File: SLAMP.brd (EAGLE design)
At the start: 160 x 100 mm, 45 parts, among them IC1 MEGA8-AI, J1 CARA1, J2 CARA4, J3 CARA2, J4 CARA5, J5 CARA3, J6 EXTRA-D12, J7 A0, Q1 2N7002PW, U1 HC_05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

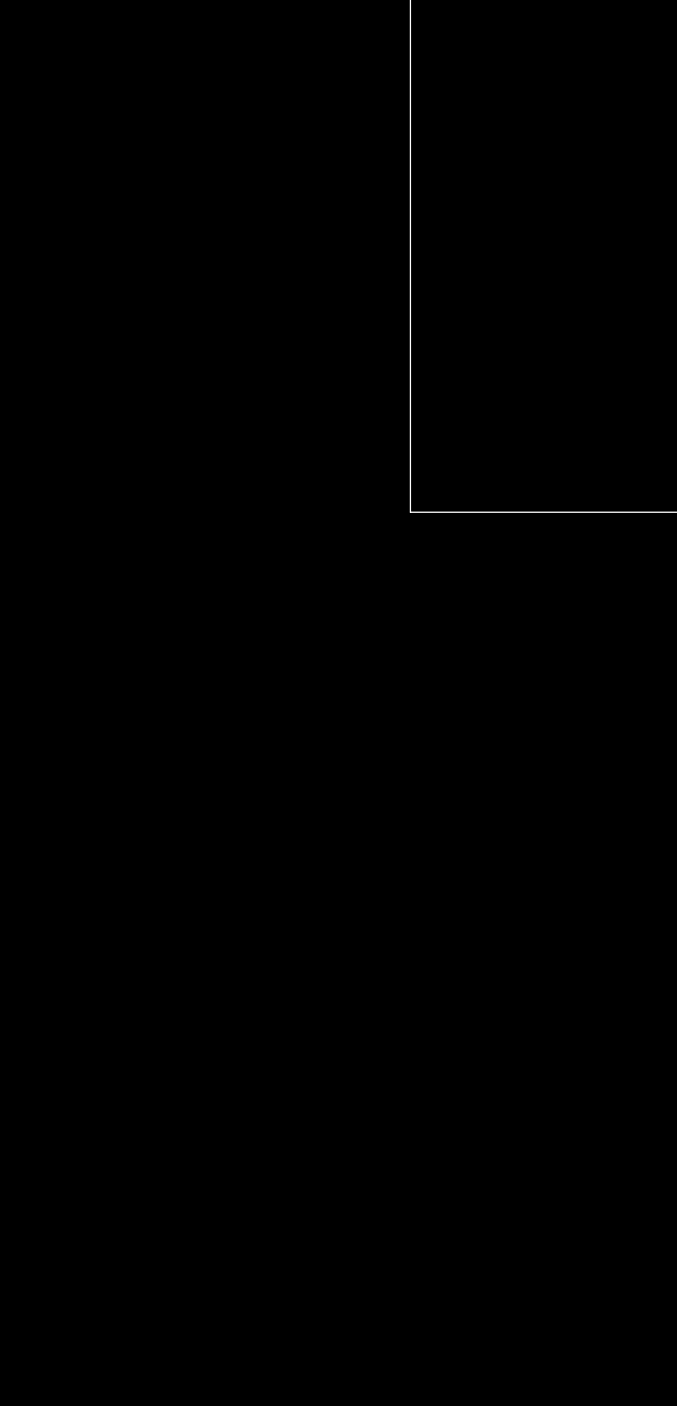
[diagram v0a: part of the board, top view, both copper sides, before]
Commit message: capacitive touch sensor added
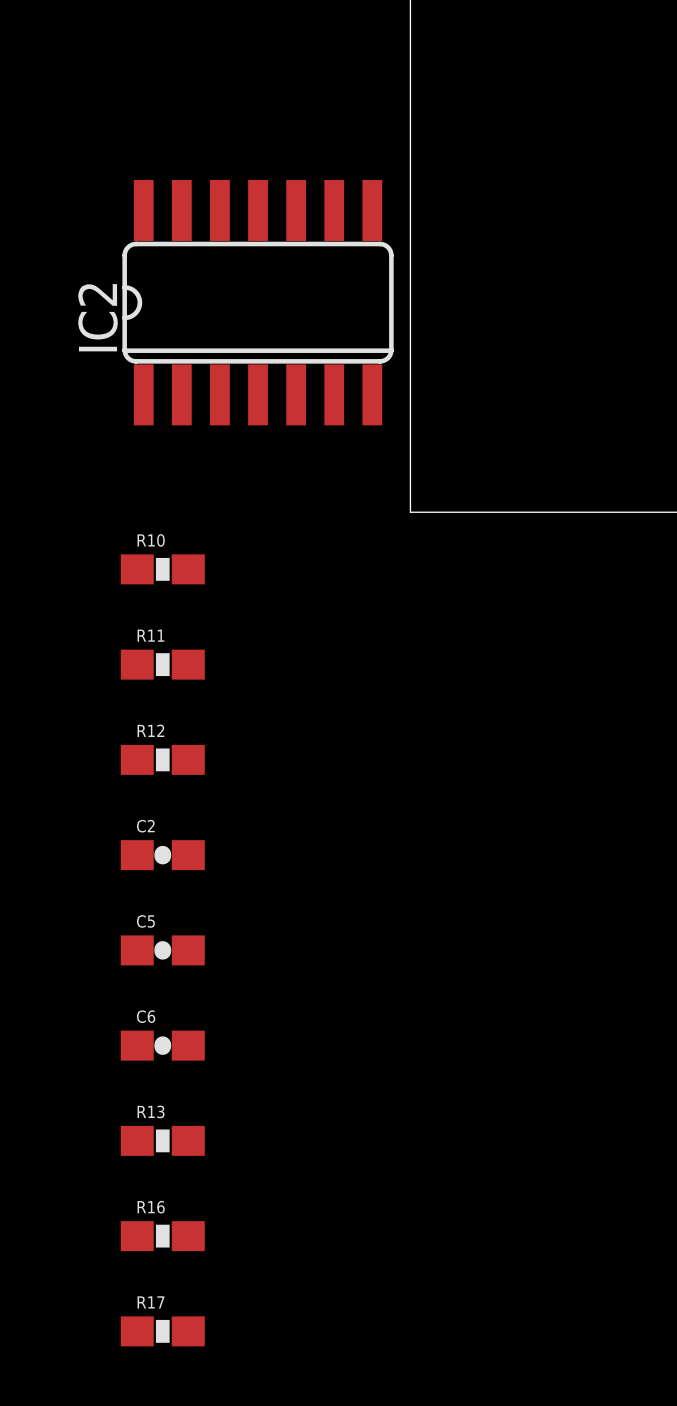
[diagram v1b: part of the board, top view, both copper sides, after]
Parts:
- added C2, C5: 1uF, SparkFun-Passives:0603-CAP
- added C6: 100nF, SparkFun-Passives:0603-CAP
- added IC2: AT42QT1070-SSU, adafruit:SO14
- added R10, R11, R12: 1k, SparkFun-Passives:0603-RES
- added R13, R16, R17: 10k, SparkFun-Passives:0603-RES
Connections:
- new net N$1: IC2.5, R17.2
- new net N$11: IC2.11, R12.1
- new net N$19: R10.2
- new net N$20: R11.2
- new net N$21: R12.2
- new net N$8: IC2.13, R10.1
- new net N$9: IC2.12, R11.1
- new net SCL: IC2.6, R16.2
- new net SDA: IC2.3, R13.2
- net 3.3V: now also C2.1, C5.1, C6.1, IC2.1, IC2.4, R13.1, R16.1, R17.1
- net GND: now also C2.2, C5.2, C6.2, IC2.14, IC2.2
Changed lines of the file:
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@@
 <?xml version="1.0" encoding="utf-8"?>
 <!DOCTYPE eagle SYSTEM "eagle.dtd">
-<eagle version="7.3.0">
+<eagle version="7.7.0">
 <drawing>
 <settings>
@@
 <attribute name="PROD_ID" value="XTAL-08900" x="42.545" y="78.105" size="1.778" layer="27" rot="R180" display="off"/>
 </element>
+<element name="IC2" library="adafruit" package="SO14" value="AT42QT1070-SSU" x="-5.08" y="6.985"/>
+<element name="R10" library="SparkFun-Passives" package="0603-RES" value="1k" x="-8.255" y="-1.905"/>
+<element name="R11" library="SparkFun-Passives" package="0603-RES" value="1k" x="-8.255" y="-5.08"/>
+<element name="R12" library="SparkFun-Passives" package="0603-RES" value="1k" x="-8.255" y="-8.255"/>
+<element name="C2" library="SparkFun-Passives" package="0603-CAP" value="1uF" x="-8.255" y="-11.43"/>
+<element name="C5" library="SparkFun-Passives" package="0603-CAP" value="1uF" x="-8.255" y="-14.605"/>
+<element name="C6" library="SparkFun-Passives" package="0603-CAP" value="100nF" x="-8.255" y="-17.78"/>
+<element name="R13" library="SparkFun-Passives" package="0603-RES" value="10k" x="-8.255" y="-20.955"/>
+<element name="R16" library="SparkFun-Passives" package="0603-RES" value="10k" x="-8.255" y="-24.13"/>
+<element name="R17" library="SparkFun-Passives" package="0603-RES" value="10k" x="-8.255" y="-27.305"/>
 </elements>
 <signals>
@@
 <wire x1="15.24" y1="78.105" x2="17.36" y2="78.105" width="0.254" layer="1"/>
 <wire x1="17.36" y1="78.105" x2="17.995" y2="78.74" width="0.254" layer="1"/>
+<wire x1="13.97" y1="43.815" x2="13.97" y2="46.62" width="0.254" layer="1"/>
+<wire x1="13.97" y1="46.62" x2="14.34" y2="46.99" width="0.254" layer="1"/>
+<wire x1="14.34" y1="46.99" x2="14.34" y2="47.255" width="0.254" layer="1"/>
+<wire x1="14.34" y1="47.255" x2="12.7" y2="48.895" width="0.254" layer="1"/>
+<wire x1="12.7" y1="48.895" x2="12.7" y2="51.435" width="0.254" layer="1"/>
+<wire x1="39.612" y1="57.15" x2="39.612" y2="59.055" width="0.254" layer="1"/>
+<wire x1="39.612" y1="59.055" x2="41.91" y2="59.055" width="0.254" layer="1"/>
+<wire x1="41.91" y1="59.055" x2="42.545" y2="59.69" width="0.254" layer="1"/>
+<wire x1="42.545" y1="59.69" x2="43.93" y2="59.69" width="0.254" layer="1"/>
+<wire x1="43.93" y1="59.69" x2="44.15" y2="59.91" width="0.254" layer="1"/>
+<wire x1="25.4" y1="77.47" x2="25.4" y2="79.07" width="0.254" layer="1"/>
+<wire x1="25.4" y1="79.07" x2="25.095" y2="79.375" width="0.254" layer="1"/>
+<contactref element="IC2" pad="14"/>
+<contactref element="IC2" pad="2"/>
+<contactref element="C2" pad="2"/>
+<contactref element="C5" pad="2"/>
+<contactref element="C6" pad="2"/>
 <wire x1="46.45" y1="85.81" x2="55.975" y2="85.81" width="0" layer="19" extent="1-1"/>
 <wire x1="42.545" y1="79.121" x2="46.45" y2="85.81" width="0" layer="19" extent="1-1"/>
@@
 <wire x1="17.995" y1="76.835" x2="24.4475" y2="76.5175" width="0" layer="19" extent="1-1"/>
 <wire x1="17.875" y1="85.81" x2="17.995" y2="80.01" width="0" layer="19" extent="1-1"/>
+<wire x1="27.4" y1="85.81" x2="25.095" y2="79.375" width="0" layer="19" extent="1-1"/>
 <wire x1="17.995" y1="68.58" x2="25.0825" y2="69.7103" width="0" layer="19" extent="1-1"/>
 <wire x1="11.9888" y1="62.5856" x2="17.995" y2="68.58" width="0" layer="19" extent="1-1"/>
-<wire x1="27.4" y1="85.81" x2="25.095" y2="79.375" width="0" layer="19" extent="1-1"/>
 <wire x1="12.7" y1="51.435" x2="11.9888" y2="62.5856" width="0" layer="19" extent="1-1"/>
-<wire x1="13.97" y1="43.815" x2="13.97" y2="46.62" width="0.254" layer="1"/>
-<wire x1="13.97" y1="46.62" x2="14.34" y2="46.99" width="0.254" layer="1"/>
-<wire x1="14.34" y1="46.99" x2="14.34" y2="47.255" width="0.254" layer="1"/>
-<wire x1="14.34" y1="47.255" x2="12.7" y2="48.895" width="0.254" layer="1"/>
-<wire x1="12.7" y1="48.895" x2="12.7" y2="51.435" width="0.254" layer="1"/>
-<wire x1="39.612" y1="57.15" x2="39.612" y2="59.055" width="0.254" layer="1"/>
-<wire x1="39.612" y1="59.055" x2="41.91" y2="59.055" width="0.254" layer="1"/>
-<wire x1="41.91" y1="59.055" x2="42.545" y2="59.69" width="0.254" layer="1"/>
-<wire x1="42.545" y1="59.69" x2="43.93" y2="59.69" width="0.254" layer="1"/>
-<wire x1="43.93" y1="59.69" x2="44.15" y2="59.91" width="0.254" layer="1"/>
-<wire x1="25.4" y1="77.47" x2="25.4" y2="79.07" width="0.254" layer="1"/>
-<wire x1="25.4" y1="79.07" x2="25.095" y2="79.375" width="0.254" layer="1"/>
+<wire x1="-8.89" y1="10.0584" x2="13.97" y2="43.815" width="0" layer="19" extent="1-1"/>
+<wire x1="-7.62" y1="3.9116" x2="-8.89" y2="10.0584" width="0" layer="19" extent="1-1"/>
+<wire x1="-7.405" y1="-11.43" x2="-7.62" y2="3.9116" width="0" layer="19" extent="1-1"/>
+<wire x1="-7.405" y1="-14.605" x2="-7.405" y2="-11.43" width="0" layer="19" extent="1-1"/>
+<wire x1="-7.405" y1="-17.78" x2="-7.405" y2="-14.605" width="0" layer="19" extent="1-1"/>
 </signal>
 <signal name="DTR">
@@
 <via x="37.465" y="67.945" extent="1-16" drill="0.6"/>
 <wire x1="37.465" y1="67.945" x2="35.775" y2="67.945" width="0.254" layer="1"/>
+<contactref element="IC2" pad="4"/>
+<contactref element="C2" pad="1"/>
+<contactref element="C5" pad="1"/>
+<contactref element="C6" pad="1"/>
+<contactref element="R13" pad="1"/>
+<contactref element="R16" pad="1"/>
+<contactref element="R17" pad="1"/>
+<contactref element="IC2" pad="1"/>
+<wire x1="-5.08" y1="3.9116" x2="22.5425" y2="65.405" width="0" layer="19" extent="1-1"/>
+<wire x1="-8.89" y1="3.9116" x2="-5.08" y2="3.9116" width="0" layer="19" extent="1-1"/>
+<wire x1="-9.105" y1="-11.43" x2="-8.89" y2="3.9116" width="0" layer="19" extent="1-1"/>
+<wire x1="-9.105" y1="-14.605" x2="-9.105" y2="-11.43" width="0" layer="19" extent="1-1"/>
+<wire x1="-9.105" y1="-17.78" x2="-9.105" y2="-14.605" width="0" layer="19" extent="1-1"/>
+<wire x1="-9.105" y1="-20.955" x2="-9.105" y2="-17.78" width="0" layer="19" extent="1-1"/>
+<wire x1="-9.105" y1="-24.13" x2="-9.105" y2="-20.955" width="0" layer="19" extent="1-1"/>
+<wire x1="-9.105" y1="-27.305" x2="-9.105" y2="-24.13" width="0" layer="19" extent="1-1"/>
 </signal>
 <signal name="B1">
@@
 <wire x1="26.9875" y1="73.66" x2="26.9875" y2="75.0697" width="0.254" layer="1"/>
 </signal>
+<signal name="N$8">
+<contactref element="IC2" pad="13"/>
+<contactref element="R10" pad="1"/>
+<wire x1="-7.62" y1="10.0584" x2="-9.105" y2="-1.905" width="0" layer="19" extent="1-1"/>
+</signal>
+<signal name="N$9">
+<contactref element="IC2" pad="12"/>
+<contactref element="R11" pad="1"/>
+<wire x1="-6.35" y1="10.0584" x2="-9.105" y2="-5.08" width="0" layer="19" extent="1-1"/>
+</signal>
+<signal name="N$11">
+<contactref element="IC2" pad="11"/>
+<contactref element="R12" pad="1"/>
+<wire x1="-5.08" y1="10.0584" x2="-9.105" y2="-8.255" width="0" layer="19" extent="1-1"/>
+</signal>
+<signal name="N$19">
+<contactref element="R10" pad="2"/>
+</signal>
+<signal name="N$20">
+<contactref element="R11" pad="2"/>
+</signal>
+<signal name="N$21">
+<contactref element="R12" pad="2"/>
+</signal>
+<signal name="SDA">
+<contactref element="IC2" pad="3"/>
+<contactref element="R13" pad="2"/>
+<wire x1="-6.35" y1="3.9116" x2="-7.405" y2="-20.955" width="0" layer="19" extent="1-1"/>
+</signal>
+<signal name="SCL">
+<contactref element="IC2" pad="6"/>
+<contactref element="R16" pad="2"/>
+<wire x1="-2.54" y1="3.9116" x2="-7.405" y2="-24.13" width="0" layer="19" extent="1-1"/>
+</signal>
+<signal name="N$1">
+<contactref element="R17" pad="2"/>
+<contactref element="IC2" pad="5"/>
+<wire x1="-3.81" y1="3.9116" x2="-7.405" y2="-27.305" width="0" layer="19" extent="1-1"/>
+</signal>
 </signals>

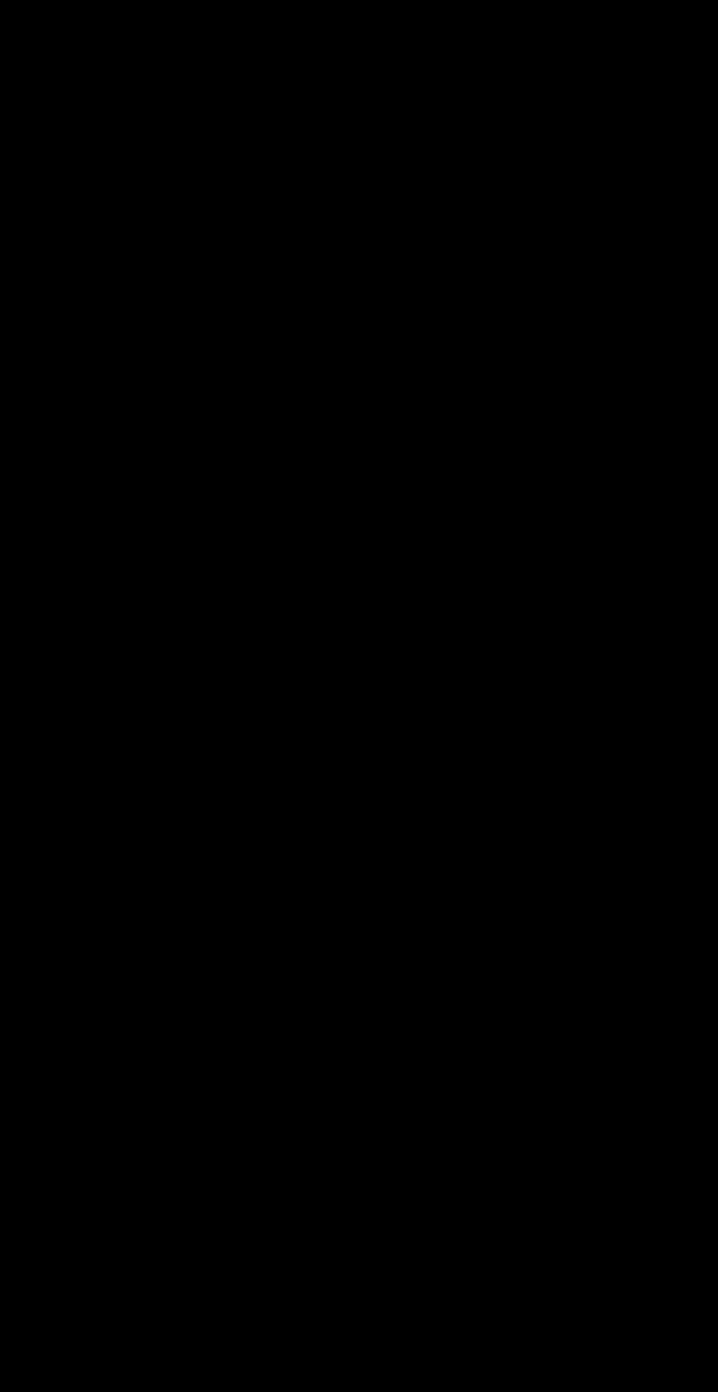
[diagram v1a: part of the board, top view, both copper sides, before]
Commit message: LM358 added
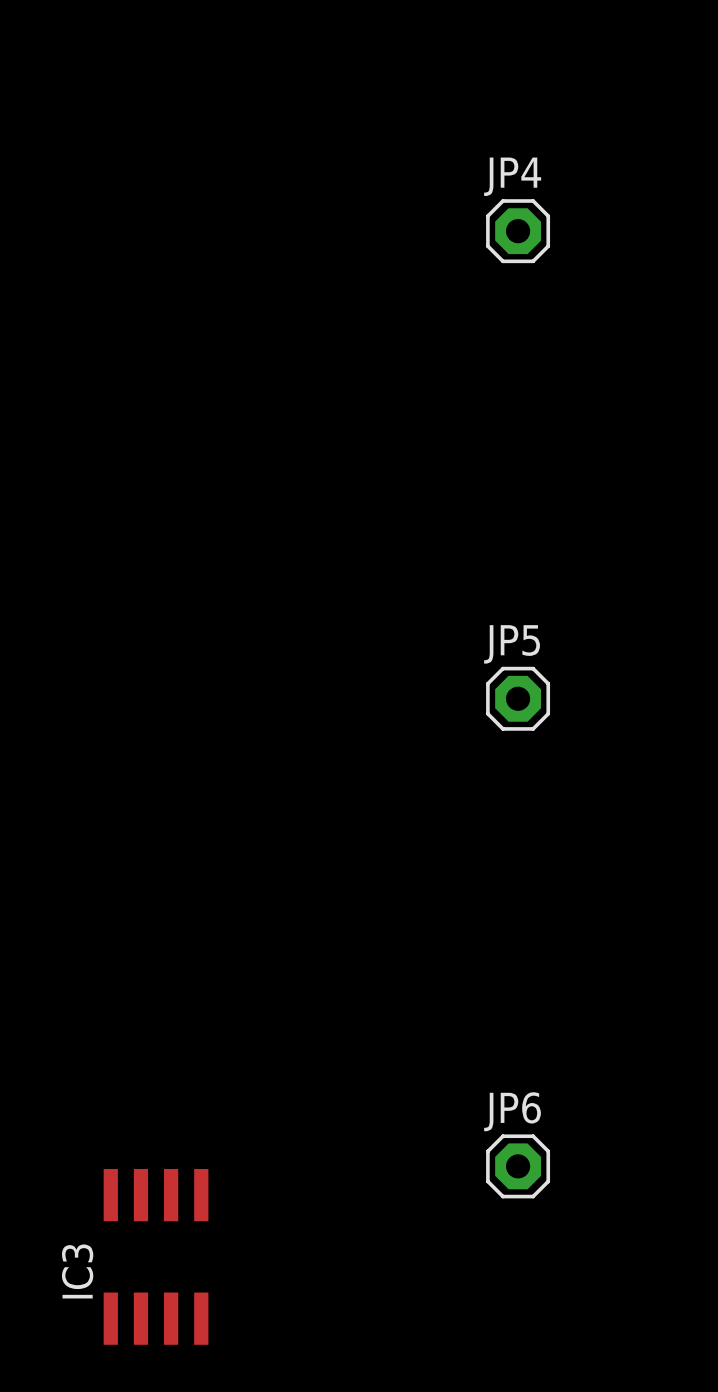
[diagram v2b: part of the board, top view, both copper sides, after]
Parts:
- added IC3: LM358D, linear:SO08
- added JP4, JP5, JP6: (no value), adafruit:1X01
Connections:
- new net V+: IC3.8
- new net V-: IC3.4
- net N$19: now also JP4.1
- net N$20: now also JP5.1
- net N$21: now also JP6.1
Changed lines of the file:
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@@
 <element name="R16" library="SparkFun-Passives" package="0603-RES" value="10k" x="-8.255" y="-24.13"/>
 <element name="R17" library="SparkFun-Passives" package="0603-RES" value="10k" x="-8.255" y="-27.305"/>
+<element name="JP4" library="adafruit" package="1X01" value="" x="-1.27" y="-38.735"/>
+<element name="JP5" library="adafruit" package="1X01" value="" x="-1.27" y="-58.42"/>
+<element name="JP6" library="adafruit" package="1X01" value="" x="-1.27" y="-78.105"/>
+<element name="IC3" library="linear" package="SO08" value="LM358D" x="-16.51" y="-81.915"/>
 </elements>
 <signals>
@@
 <signal name="N$19">
 <contactref element="R10" pad="2"/>
+<contactref element="JP4" pad="1"/>
+<wire x1="-7.405" y1="-1.905" x2="-1.27" y2="-38.735" width="0" layer="19" extent="1-1"/>
 </signal>
 <signal name="N$20">
 <contactref element="R11" pad="2"/>
+<contactref element="JP5" pad="1"/>
+<wire x1="-7.405" y1="-5.08" x2="-1.27" y2="-58.42" width="0" layer="19" extent="1-1"/>
 </signal>
 <signal name="N$21">
 <contactref element="R12" pad="2"/>
+<contactref element="JP6" pad="1"/>
+<wire x1="-7.405" y1="-8.255" x2="-1.27" y2="-78.105" width="0" layer="19" extent="1-1"/>
 </signal>
 <signal name="SDA">
@@
 <wire x1="-3.81" y1="3.9116" x2="-7.405" y2="-27.305" width="0" layer="19" extent="1-1"/>
 </signal>
+<signal name="V+">
+<contactref element="IC3" pad="8"/>
+</signal>
+<signal name="V-">
+<contactref element="IC3" pad="4"/>
+</signal>
 </signals>

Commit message: Making some changes
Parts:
- removed IC3: LM358D, linear:SO08
- removed JP6: (no value), adafruit:1X01
- removed R1: 2k, SparkFun-Passives:0805
- removed U5: MIC5219 3.3V, SparkFun-PowerIC:SOT23-5
- added R26: 10k, SparkFun-Passives:0603-RES
- added U3: MIC5219 3.3V, SparkFun-PowerIC:SOT23-5
- C1, C3: value 0.1u -> 100n
- C10, C11: value 0.1u -> 1uF
- C15: value 10u -> 100nF; device rcl:SMC_P -> SparkFun-Passives:0603-CAP
- C2, C5: value 1uF -> 0.1u
- C6: value 100nF -> 10u; device SparkFun-Passives:0603-CAP -> rcl:SMC_P
- JP2: value CTS/RTS-bt -> (none); device pinhead:1X02 -> adafruit:1X01
- LED1: value RX -> TX
- LED2: value TX -> RX
- R13: value 10k -> 1k
- R3: value 330 -> 1k
- R7: value 1k -> 2k; device SparkFun-Passives:0603-RES -> SparkFun-Passives:0805
- moved C15 271.3 mm to (-15.9, -188.6), turned to 0 degrees
- moved C11 256.3 mm to (-21.6, -188.6), turned to 0 degrees
- moved R8 255.5 mm to (-10.2, -188.6), turned to 0 degrees
- moved LED2 252.7 mm to (-11.4, -184.8), turned to 0 degrees
- moved LED1 251.9 mm to (-16.5, -184.8), turned to 0 degrees
- moved C10 242.3 mm to (14.0, -181.6)
- moved R7 207.6 mm to (-22.9, -138.4), turned to 0 degrees
- moved JP2 202.3 mm to (-14.6, -150.5), turned to 0 degrees
- moved R10 186.7 mm to (-4.45, -188.6)
- moved R11 183.8 mm to (1.27, -188.6)
- moved R12 181.0 mm to (6.99, -188.6)
- moved IC2 174.1 mm to (1.91, -167.0)
- moved C2 170.5 mm to (2.54, -181.6)
- moved R13 168.9 mm to (12.7, -188.6)
- moved R16 168.2 mm to (-21.6, -191.8)
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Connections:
- net B1 renamed B_TX
- net B2 renamed B_RX
- removed net CTS: JP2.1, U1.3
- removed net RTS: JP2.2, U1.4
- removed net STATE: R1.1, U1.31
- removed net V+: IC3.8
- removed net V-: IC3.4
- new net BT_RX: IC1.1
- new net BT_TX: IC1.32
- new net D7: IC1.11
- new net D8: IC1.12
- new net N$22: IC1.22
- new net N$30: IC2.5, R26.2
- new net N$7: IC1.19
- net 3.3V: now also C10.1, C15.1, C6.+, R26.1, U3.5; no longer C15.+, C2.1, C6.1, R13.1, U5.5
- net 5V: now also C2.2, U3.1, U3.3; no longer C10.2, U5.1, U5.3
- net CBUS1: now also LED2.C; no longer LED1.C
- net CBUS2: now also LED1.C; no longer LED2.C
- net D12: no longer IC1.16
- net D2: no longer IC1.32
- net D3: no longer IC1.1
- net GND: now also C10.2, C15.2, C2.1, C6.-, U3.2; no longer C10.1, C15.-, C2.2, C6.2, U1.21, U5.2
- net KEY: no longer U1.34
- net N$1: now also R7.1, U1.24; no longer IC2.5, R17.2
- net N$10: now also LED2.A, R10.1; no longer D1.A, R1.2
- net N$11: now also IC2.13, R11.1; no longer IC2.11, R12.1
- net N$12: now also IC2.12, R12.1; no longer LED2.A, R8.1
- net N$13: now also IC2.11, R13.1; no longer LED1.A, R7.1
- net N$19: now also JP2.1, R11.2; no longer JP4.1, R10.2
- net N$20: now also JP4.1, R12.2; no longer JP5.1, R11.2
- net N$21: now also JP5.1, R13.2; no longer JP6.1, R12.2
- net N$8: now also D1.A, R7.2; no longer IC2.13, R10.1
- net N$9: now also LED1.A, R8.1; no longer IC2.12, R11.1
- net SCL: now also R17.2; no longer R16.2
- net SDA: now also R16.2; no longer R13.2
- net VCCIO: now also R10.2; no longer R7.2
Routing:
- net CTS: track 18.6 -> 0.00 mm, vias 1 -> 0
- net RTS: track 18.1 -> 0.00 mm, vias 1 -> 0
- net STATE: track 16.3 -> 0.00 mm
- net 5V: track 240.0 -> 226.9 mm
- net GND: track 35.8 -> 27.8 mm
- net 3.3V: track 66.0 -> 60.7 mm
- net N$13: track 2.21 -> 0.00 mm
- net N$12: track 2.21 -> 0.00 mm
- net N$10: track 2.03 -> 0.00 mm
- net VCCIO: track 1.91 -> 0.00 mm
- net CBUS2: track 29.1 -> 27.3 mm
- net CBUS1: track 22.0 -> 20.2 mm
- net D5: track 24.2 -> 23.1 mm
